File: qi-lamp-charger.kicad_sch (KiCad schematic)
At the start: 27 parts

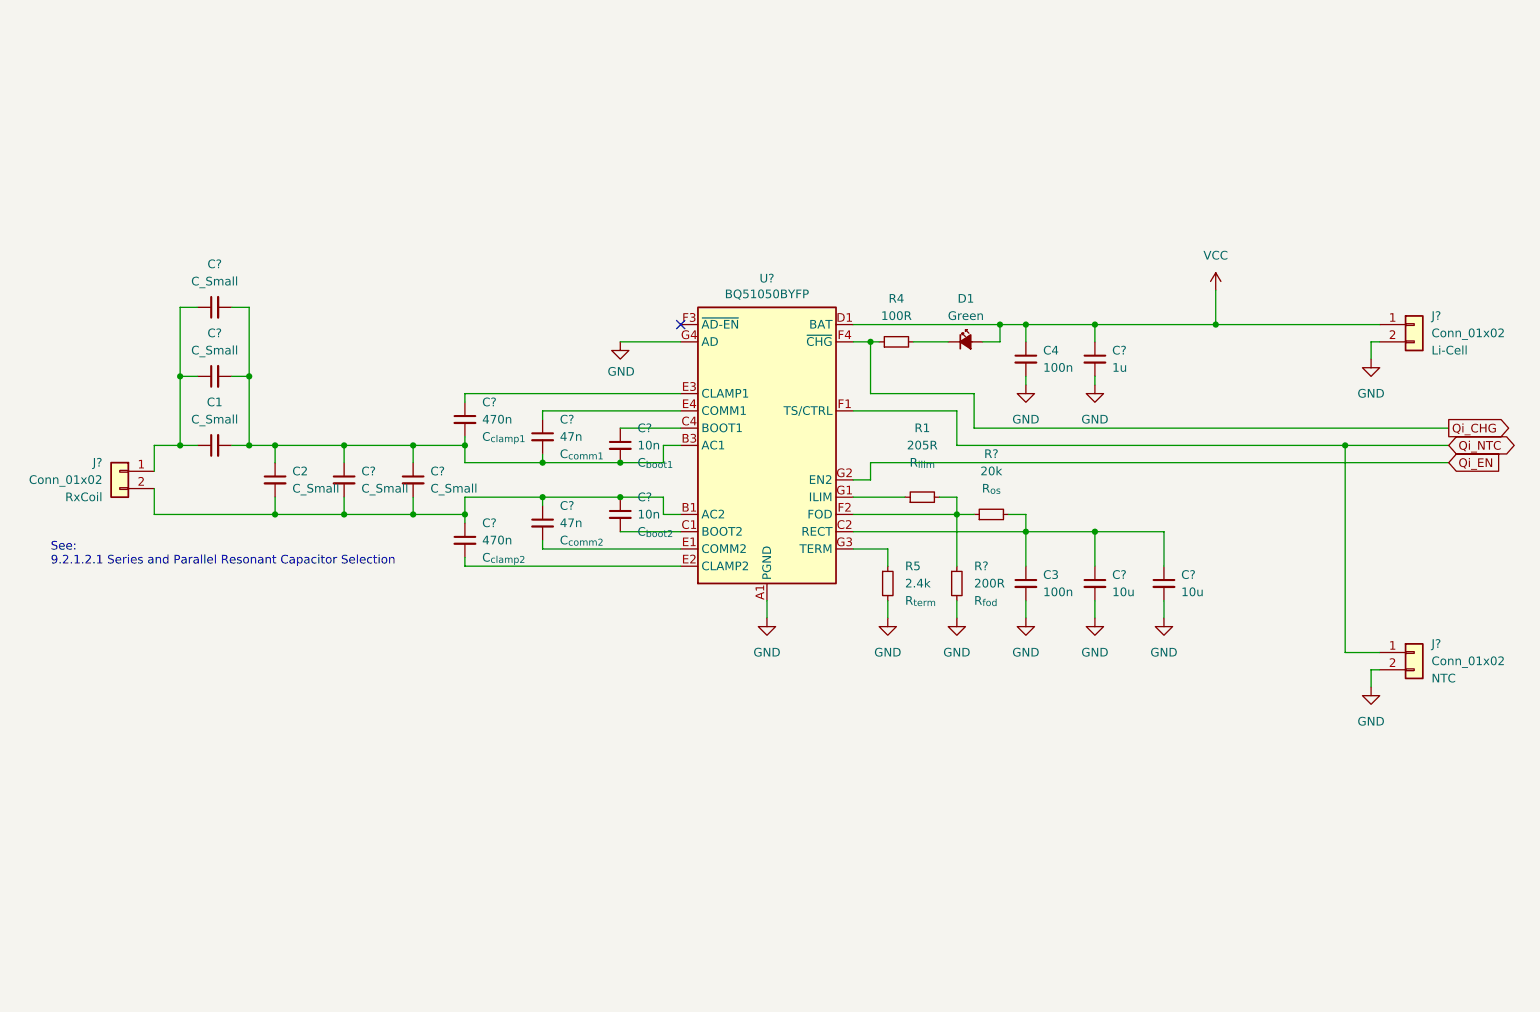
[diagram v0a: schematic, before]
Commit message: add esp8266
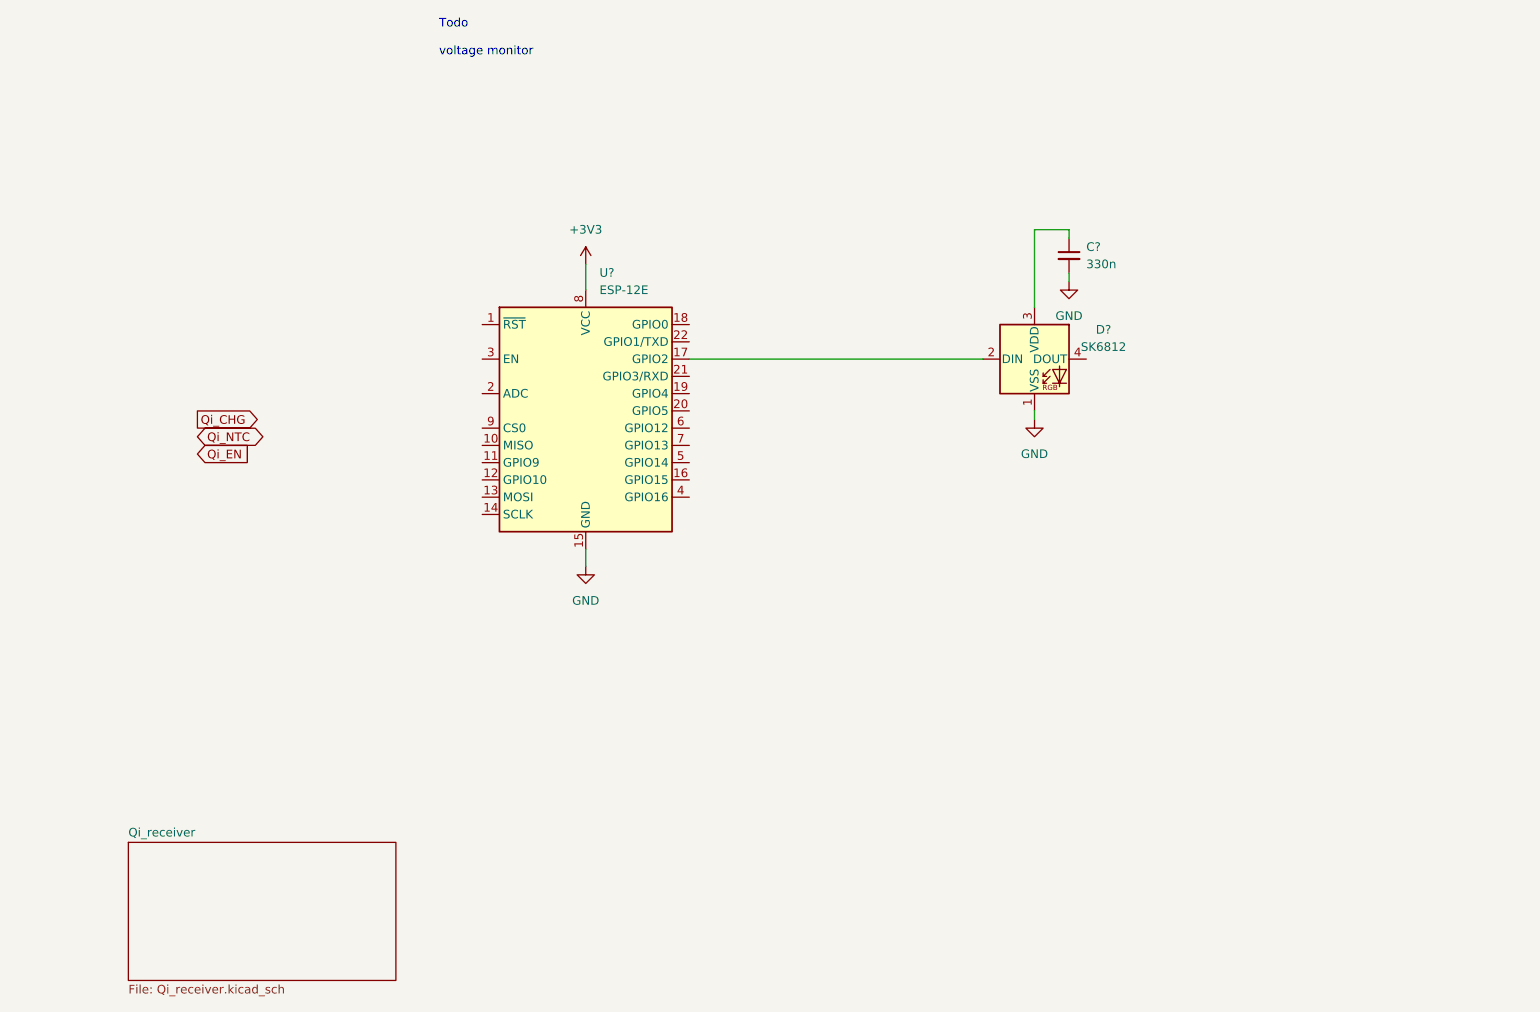
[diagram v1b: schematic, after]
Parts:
- removed C1, C2, C? (x4): C_Small, Capacitor_SMD:C_0603_1608Metric, symbol Device:C_Small
- removed C3, C4: 100n, Capacitor_SMD:C_0603_1608Metric, symbol Device:C_Small
- removed C? (x2): 47n, Capacitor_SMD:C_0603_1608Metric, symbol Device:C_Small
- removed C? (x2): 470n, Capacitor_SMD:C_0603_1608Metric, symbol Device:C_Small
- removed C? (x2): 10n, Capacitor_SMD:C_0603_1608Metric, symbol Device:C_Small
- removed C? (x2): 10u, Capacitor_SMD:C_0805_2012Metric, symbol Device:C_Small
- removed C?: 1u, Capacitor_SMD:C_0603_1608Metric, symbol Device:C_Small
- removed D1: Green, LED_SMD:LED_0603_1608Metric, symbol Device:LED_Small_Filled
- removed J? (x3): Conn_01x02, Connector_PinHeader_2.54mm:PinHeader_1x02_P2.54mm_Vertical, symbol Connector_Generic:Conn_01x02
- removed R1: 205R, Resistor_SMD:R_0603_1608Metric, symbol Device:R_Small
- removed R4: 100R, Resistor_SMD:R_0603_1608Metric, symbol Device:R_Small
- removed R5: 2.4k, Resistor_SMD:R_0603_1608Metric, symbol Device:R_Small
- removed R?: 20k, Resistor_SMD:R_0603_1608Metric, symbol Device:R_Small
- removed R?: 200R, Resistor_SMD:R_0603_1608Metric, symbol Device:R_Small
- removed U?: BQ51050BYFP, Package_BGA:Texas_DSBGA-28_1.9x3.0mm_Layout4x7_P0.4mm, symbol Battery_Management:BQ51050BYFP
- added C?: 330n, Capacitor_SMD:C_0603_1608Metric, symbol Device:C_Small
- added D?: SK6812, LED_SMD:LED_SK6812_PLCC4_5.0x5.0mm_P3.2mm, symbol LED:SK6812
- added U?: ESP-12E, RF_Module:ESP-12E, symbol RF_Module:ESP-12E
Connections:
- net GND: now also C?.2, D?.1 (VSS), U?.15 (GND)
- new net: D?.2 (DIN), U?.17 (GPIO2)
- new net: C?.1, D?.3 (VDD)
- new net +3V3: U?.8 (VCC)
- no-connect marks 1 -> 0
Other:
- added sheet Qi_receiver (Qi_receiver.kicad_sch)
- note added: "Todo voltage monitor"
- note removed: "See: 9.2.1.2.1 Series and Parallel Resonant Capacitor Selection"

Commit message: Add power switch & LED's & ESP_GPIO's
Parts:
- added C1, C2, C? (x4): C_Small, Capacitor_SMD:C_0603_1608Metric, symbol Device:C_Small
- added C3, C4, C? (x3): 100n, Capacitor_SMD:C_0603_1608Metric, symbol Device:C_Small
- added C? (x2): 47n, Capacitor_SMD:C_0603_1608Metric, symbol Device:C_Small
- added C? (x11): 330n, Capacitor_SMD:C_0603_1608Metric, symbol Device:C_Small
- added C? (x2): 10u, Capacitor_SMD:C_0805_2012Metric, symbol Device:C_Small
- added C? (x2): 10n, Capacitor_SMD:C_0603_1608Metric, symbol Device:C_Small
- added C? (x2): 470n, Capacitor_SMD:C_0603_1608Metric, symbol Device:C_Small
- added C?: 1u, Capacitor_SMD:C_0603_1608Metric, symbol Device:C_Small
- added D1: Green, LED_SMD:LED_0603_1608Metric, symbol Device:LED_Small_Filled
- added D? (x9): SK6812, LED_SMD:LED_SK6812_PLCC4_5.0x5.0mm_P3.2mm, symbol LED:SK6812
- added J?: Conn_01x03, Connector_PinHeader_2.54mm:PinHeader_1x03_P2.54mm_Vertical, symbol Connector_Generic:Conn_01x03
- added J? (x3): Conn_01x02, Connector_PinHeader_2.54mm:PinHeader_1x02_P2.54mm_Vertical, symbol Connector_Generic:Conn_01x02
- added JP? (x10): SolderJumper_2_Open, symbol Jumper:SolderJumper_2_Open
- added Q?: Q_PMOS_GDS, symbol Device:Q_PMOS_GDS
- added R1: 205R, Resistor_SMD:R_0603_1608Metric, symbol Device:R_Small
- added R4: 100R, Resistor_SMD:R_0603_1608Metric, symbol Device:R_Small
- added R5: 2.4k, Resistor_SMD:R_0603_1608Metric, symbol Device:R_Small
- added R?: 20k, Resistor_SMD:R_0603_1608Metric, symbol Device:R_Small
- added R?: 200R, Resistor_SMD:R_0603_1608Metric, symbol Device:R_Small
- added U?: BQ51050BYFP, Package_BGA:Texas_DSBGA-28_1.9x3.0mm_Layout4x7_P0.4mm, symbol Battery_Management:BQ51050BYFP
- added U?: SLG5NV1430V, symbol Kharars-KiCAD-lib:SLG5NV1430V
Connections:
- net +3V3 is gone; now on net VCC: U?.8 (VCC)
- net GND: now also C3.2, C4.2, C?.2, C?.2, C?.2, C?.2, C?.2, C?.2, C?.2, C?.2, C?.2, C?.2, C?.2, C?.2, C?.2, C?.2, C?.2, C?.2, C?.2, D?.1 (VSS), D?.1 (VSS), D?.1 (VSS), D?.1 (VSS), D?.1 (VSS), D?.1 (VSS), D?.1 (VSS), D?.1 (VSS), D?.1 (VSS), J?.2 (Pin_2), J?.2 (Pin_2), J?.3 (Pin_3), R5.2, R?.2, U?.8 (GND), U?.A1 (PGND), U?.A2 (PGND), U?.A3 (PGND), U?.A4 (PGND), U?.G2 (EN2), U?.G4 (AD)
- net Qi_NTC: now also U?.2 (ADC), J?.1 (Pin_1), U?.F1 (TS/CTRL)
- net ~{ESP_RST}: now reaches U?.1 (~{RST})
- net ESP_DOUT: now reaches D?.2 (DIN), U?.17 (GPIO2)
- net ESP_DOUT: now also J?.2 (Pin_2), JP?.1 (A)
- net ESP_GPIO0: now reaches U?.18 (GPIO0)
- net ~{PWR_OFF}: now reaches U?.19 (GPIO4)
- net ~{PWR_OFF}: now also C?.1, Q?.2 (D), U?.2 (ON)
- net ~{Qi_CHG}: now reaches U?.20 (GPIO5)
- net ~{Qi_CHG}: now also R4.1, U?.F4 (~{CHG})
- net ESP_RXD: now reaches U?.21 (GPIO3/RXD)
- net ESP_TXD: now reaches U?.22 (GPIO1/TXD)
- net ESP_EN: now reaches U?.3 (EN)
- net LED_DOUT: now reaches U?.6 (GPIO12)
- net LED_DOUT: now also D?.4 (DOUT), JP?.2 (B)
- net VCC: now reaches C?.1, D?.3 (VDD)
- net VCC: now also C?.1, C?.1, C?.1, C?.1, C?.1, C?.1, C?.1, C?.1, C?.1, C?.1, C?.1, D?.3 (VDD), D?.3 (VDD), D?.3 (VDD), D?.3 (VDD), D?.3 (VDD), D?.3 (VDD), D?.3 (VDD), D?.3 (VDD), D?.3 (VDD), J?.1 (Pin_1), U?.5 (S), U?.6 (S)
- net at D?.4 (DOUT): now also D?.2 (DIN), JP?.1 (A), JP?.2 (B)
- new net: D?.2 (DIN), D?.4 (DOUT), JP?.1 (A), JP?.2 (B) (x8)
- new net: C2.2, C?.1, C?.1, C?.1, C?.2, C?.2, J?.2 (Pin_2), U?.B1 (AC2), U?.B2 (AC2)
- new net: C?.2, U?.E1 (COMM2)
- new net: C3.1, C?.1, C?.1, R?.2, U?.C2 (RECT), U?.C3 (RECT)
- new net: C1.2, C2.1, C?.1, C?.1, C?.2, C?.2, C?.2, C?.2, C?.2, U?.B3 (AC1), U?.B4 (AC1)
- new net: C?.2, U?.C1 (BOOT2)
- new net: C?.1, U?.C4 (BOOT1)
- new net: C?.2, U?.E2 (CLAMP2)
- new net: C?.1, U?.E3 (CLAMP1)
- new net: C?.1, U?.E4 (COMM1)
- new net: R1.2, R?.1, R?.1, U?.F2 (FOD)
- new net: R1.1, U?.G1 (ILIM)
- new net: R5.1, U?.G3 (TERM)
- new net: C?.1, U?.7 (CAP)
- new net: C1.1, C?.1, C?.1, J?.1 (Pin_1)
- new net: D1.1 (K), R4.2
- new net +BATT: C4.1, C?.1, C?.1, D1.2 (A), J?.1 (Pin_1), Q?.3 (S), U?.1 (VDD), U?.3 (D), U?.4 (D), U?.D1 (BAT), U?.D2 (BAT), U?.D3 (BAT), U?.D4 (BAT)
- new net Qi_~{CHG}: Q?.1 (G)
- no-connect marks 0 -> 11
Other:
- removed sheet Qi_receiver
- note added: "100n gives around 1 second to reach V_{ON} < 0.3 V through internal 4 MΩ pull down resistor"
- note added: "See: 9.2.1.2.1 Series and Parallel Resonant Capacitor Selection"
- note removed: "Todo voltage monitor"
- moved on the sheet: C?, D?, U?

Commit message: Schematic done - missing just two footprints
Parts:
- removed C?: 330n, Capacitor_SMD:C_0603_1608Metric, symbol Device:C_Small
- added C13: 100n, Capacitor_SMD:C_0603_1608Metric, symbol Device:C_Small
- added C22: 10u, Capacitor_SMD:C_0805_2012Metric, symbol Device:C_Small
- added J4: Conn_01x06, Connector_PinHeader_2.54mm:PinHeader_1x06_P2.54mm_Vertical, symbol Connector_Generic:Conn_01x06
- added JP1, JP3, JP4: SolderJumper_2_Bridged, Jumper:SolderJumper-2_P1.3mm_Bridged_RoundedPad1.0x1.5mm, symbol Jumper:SolderJumper_2_Bridged
- added JP2: SolderJumper_2_Open, Jumper:SolderJumper-2_P1.3mm_Open_RoundedPad1.0x1.5mm, symbol Jumper:SolderJumper_2_Open
- added R10, R11, R13, R9: 10k, Resistor_SMD:R_0603_1608Metric, symbol Device:R_Small
- added R12: 0R, Resistor_SMD:R_0603_1608Metric, symbol Device:R_Small
- added R2: 20k, Resistor_SMD:R_0603_1608Metric, symbol Device:R_Small
- added R3, R6: R, Resistor_SMD:R_0603_1608Metric, symbol Device:R_Small
- C10: renamed from C?; Name C_{comm1} -> (none); silk_text (none) -> C_{comm1}
- C11: renamed from C?; Name C_{boot1} -> (none); silk_text (none) -> C_{boot1}
- C17: renamed from C?; Name C_{boot2} -> (none); silk_text (none) -> C_{boot2}
- C18: renamed from C?; Name C_{comm2} -> (none); silk_text (none) -> C_{comm2}
- C19: renamed from C?; Name C_{clamp2} -> (none); silk_text (none) -> C_{clamp2}
- C9: renamed from C?; Name C_{clamp1} -> (none); silk_text (none) -> C_{clamp1}
- JP10, JP11, JP12, JP13, JP14, JP5, JP6, JP7, JP8, JP9: renamed from JP?; footprint (none) -> Jumper:SolderJumper-2_P1.3mm_Open_RoundedPad1.0x1.5mm
- R1: Name R_{ilim} -> (none); silk_text (none) -> R_{ilim}
- R5: Name R_{term} -> (none); silk_text (none) -> R_{term}
- R7: renamed from R?; Name R_{os} -> (none); silk_text (none) -> R_{os}
- R8: renamed from R?; Name R_{fod} -> (none); silk_text (none) -> R_{fod}
- gave numbers to parts that had none: 39
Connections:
- net Qi_~{CHG} is gone; now on net ~{Qi_CHG}: Q1.1 (G)
- net +BATT: now also R2.1
- net ESP_GPIO0: now also JP3.1 (A)
- net ESP_RXD: now also J4.4 (Pin_4)
- net ESP_TXD: now also J4.5 (Pin_5)
- net GND: now also C13.2, C22.2, J4.1 (Pin_1), R12.1, R13.1, R6.2
- net Qi_NTC: now also R3.2; no longer U2.F1 (TS/CTRL)
- net VCC: now also C22.1, JP2.1 (A), JP4.1 (A), R10.2, R11.2, R9.2; no longer C24.1, C25.1, C26.1, C27.1, C28.1, C29.1, C30.1, C31.1, C32.1, C33.1, D10.3 (VDD), D11.3 (VDD), D2.3 (VDD), D3.3 (VDD), D4.3 (VDD), D5.3 (VDD), D6.3 (VDD), D7.3 (VDD), D8.3 (VDD), D9.3 (VDD)
- net ~{ESP_RST}: now also JP1.1 (A)
- net at U3.16 (GPIO15): now also R13.2
- net ESP_DOUT renamed LED_DIN
- net ESP_EN: no longer names the net of U3.3 (EN)
- net ESP_EN: now also R9.1
- new net: C24.1, C25.1, C26.1, C27.1, C28.1, C29.1, C30.1, C31.1, C32.1, C33.1, D10.3 (VDD), D11.3 (VDD), D2.3 (VDD), D3.3 (VDD), D4.3 (VDD), D5.3 (VDD), D6.3 (VDD), D7.3 (VDD), D8.3 (VDD), D9.3 (VDD), JP4.2 (B)
- new net: C13.1, R2.2, R3.1, R6.1, U2.F1 (TS/CTRL)
- new net 3V3: J4.3 (Pin_3), JP2.2 (B)
- new net DTR: J4.2 (Pin_2), JP3.2 (B), R11.1, R12.2
- new net RTS: J4.6 (Pin_6), JP1.2 (B), R10.1
- no-connect marks 11 -> 10
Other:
- note added: "GND DTR VCC ESP_RXD ESP_TXD RTS"
- note added: "Programming reference: https://circuitjournal.com/esp8266-with-arduino-ide"
- moved on the sheet: C1, C10, C11, C12, C14, C15, C16, C17, C18, C19, C2, C20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
